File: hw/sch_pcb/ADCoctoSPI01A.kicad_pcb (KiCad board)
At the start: 2 copper layers, 70.6 x 70.6 mm, 79 parts, among them J1 +5V, J10 HEADER_1x02, J11 HEADER_2x04, J2 SATA7-67491-1030, J3 SATA7-67491-1030, J4 SATA7-67491-1030, J5 SATA7-67491-1030, J6 SAS_mini_1888174, J7 SATA7-67491-1030, J8 HEADER_1x02, J9 HEADER_1x02, M1 HOLE, M2 HOLE, M3 HOLE, M4 HOLE, U1 AFE5801, U2 LM1117MP-1,8/NO, U3 LM1117MP-3,3/NO

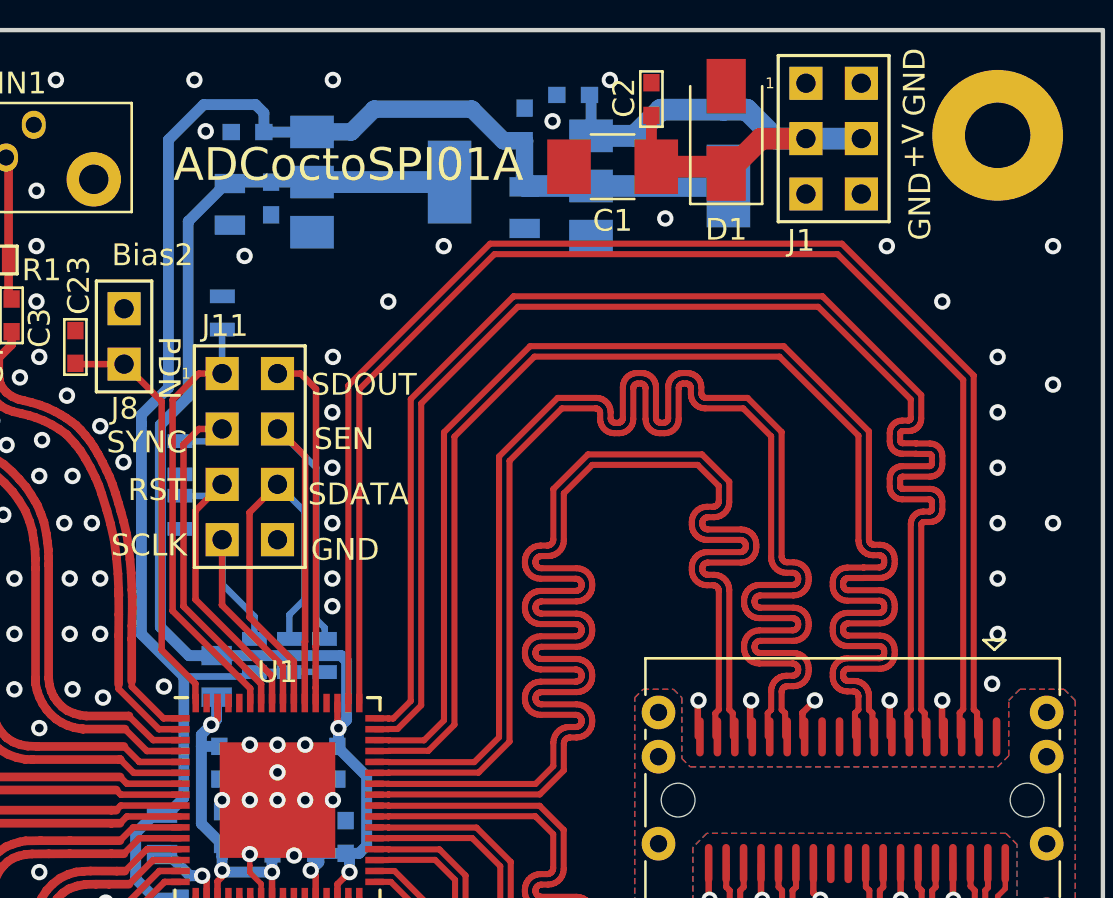
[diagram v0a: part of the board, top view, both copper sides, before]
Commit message: Update miniSAS connector footprint.
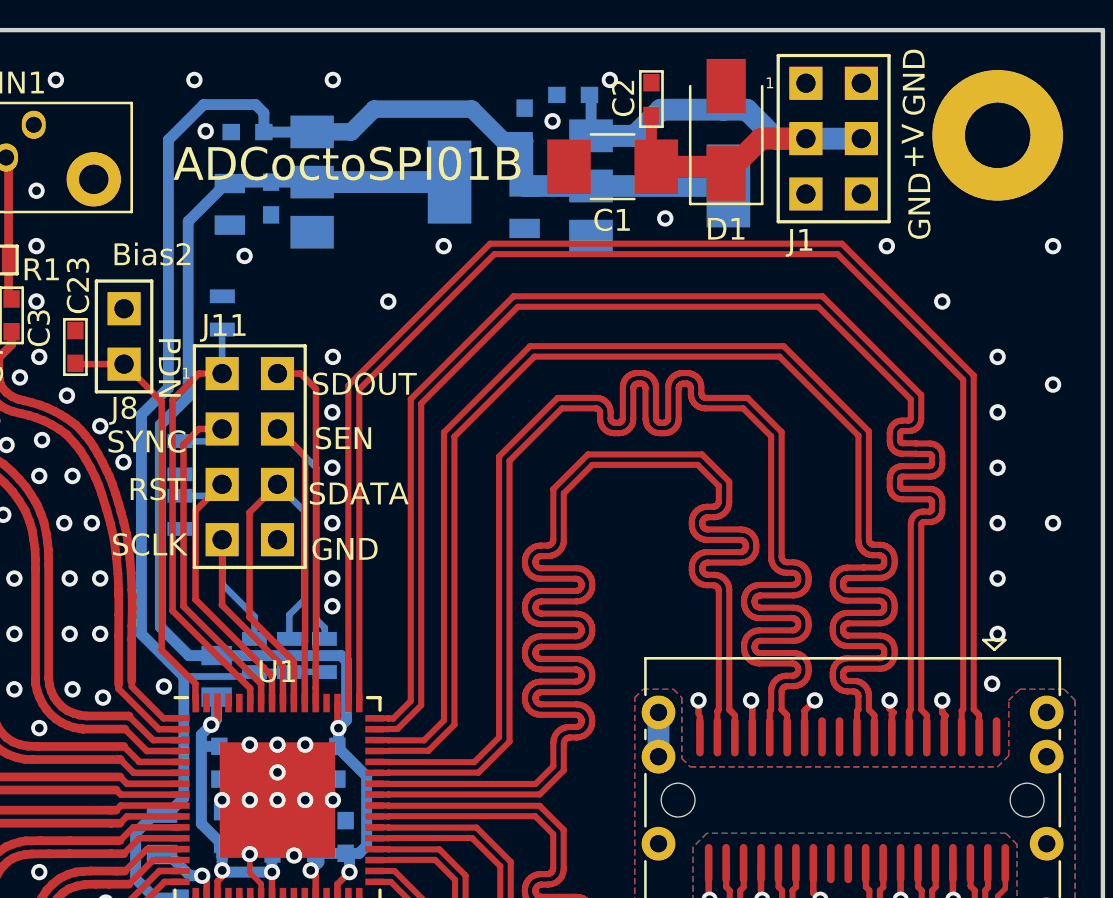
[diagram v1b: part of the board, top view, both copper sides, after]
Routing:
- net Net-(C24-Pad2): track 0.00 -> 2.03 mm
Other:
- board text added: "ADCoctoSPI01B"
- board text removed: "ADCoctoSPI01A"
